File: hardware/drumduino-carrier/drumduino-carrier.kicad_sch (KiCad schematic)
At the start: 49 parts, among them J1 IN A0 CRASH, J10 IN A9 RIDE BELL, J11 IN A10 AUX, J12 IN A11 AUX, J13 IN A12 AUX, J14 IN A13 AUX, J15 IN A14 AUX, J16 HH PEDAL (wiper/VCC/GND), J2 IN A1 HIHAT, J3 IN A2 SNARE, J4 IN A3 KICK, J5 IN A4 TOM1, J6 IN A5 TOM2, J7 IN A6 FLOOR, J8 IN A7 RIDE, J9 IN A8 SN RIM, U1 MEGA2560_PRO

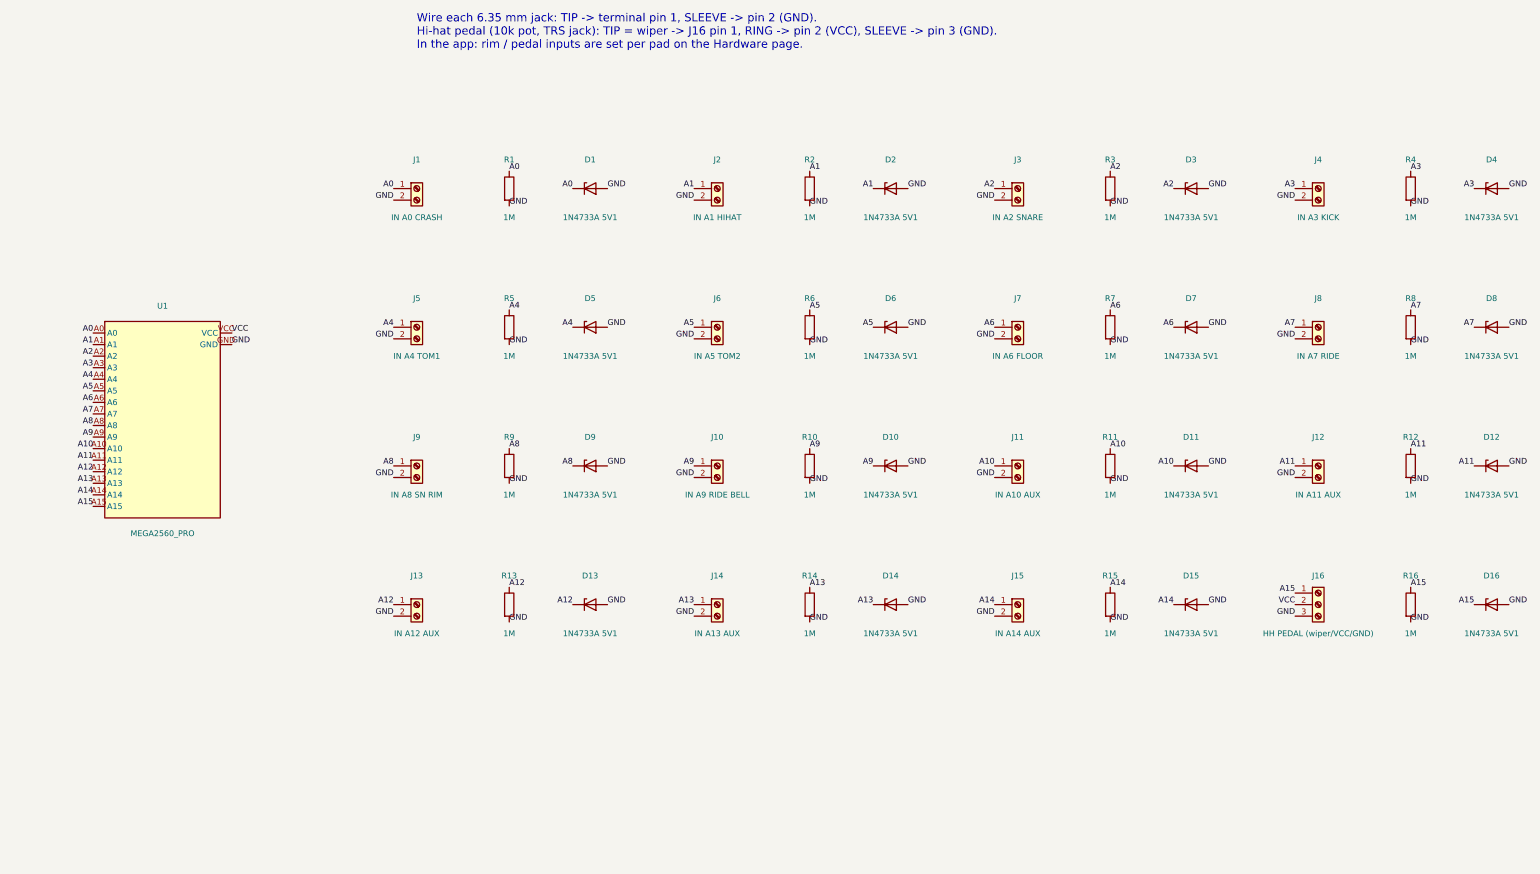
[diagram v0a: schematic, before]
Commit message: Carrier v2: 16 Rean NRJ6HF edge jacks, DC 9V input with 1N5819, local 3D models (incl. Mega 2560 PRO)
Co-Authored-By: Claude Opus 5.5 <noreply@anthropic.com>
Claude-Session: https://claude.ai/code/session_019Dkdmctnzo4hmTgGEA8k6P
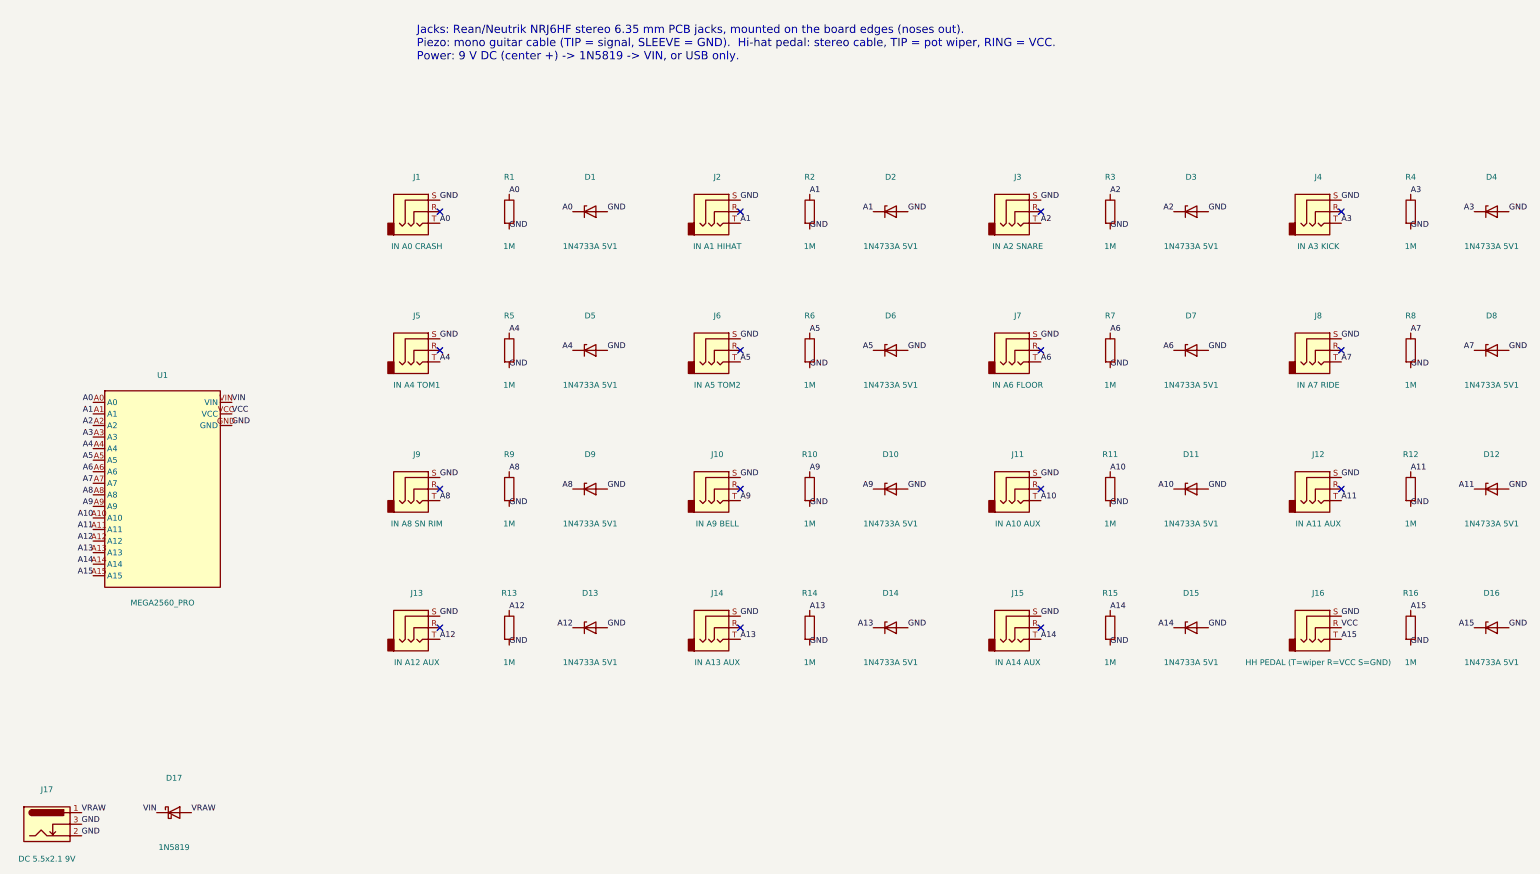
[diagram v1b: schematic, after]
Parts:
- removed J1: IN A0 CRASH, TerminalBlock_Phoenix:TerminalBlock_Phoenix_MKDS-1,5-2-5.08_1x02_P5.08mm_Horizontal, symbol Connector:Screw_Terminal_01x02
- removed J10: IN A9 RIDE BELL, TerminalBlock_Phoenix:TerminalBlock_Phoenix_MKDS-1,5-2-5.08_1x02_P5.08mm_Horizontal, symbol Connector:Screw_Terminal_01x02
- removed J11: IN A10 AUX, TerminalBlock_Phoenix:TerminalBlock_Phoenix_MKDS-1,5-2-5.08_1x02_P5.08mm_Horizontal, symbol Connector:Screw_Terminal_01x02
- removed J12: IN A11 AUX, TerminalBlock_Phoenix:TerminalBlock_Phoenix_MKDS-1,5-2-5.08_1x02_P5.08mm_Horizontal, symbol Connector:Screw_Terminal_01x02
- removed J13: IN A12 AUX, TerminalBlock_Phoenix:TerminalBlock_Phoenix_MKDS-1,5-2-5.08_1x02_P5.08mm_Horizontal, symbol Connector:Screw_Terminal_01x02
- removed J14: IN A13 AUX, TerminalBlock_Phoenix:TerminalBlock_Phoenix_MKDS-1,5-2-5.08_1x02_P5.08mm_Horizontal, symbol Connector:Screw_Terminal_01x02
- removed J15: IN A14 AUX, TerminalBlock_Phoenix:TerminalBlock_Phoenix_MKDS-1,5-2-5.08_1x02_P5.08mm_Horizontal, symbol Connector:Screw_Terminal_01x02
- removed J16: HH PEDAL (wiper/VCC/GND), TerminalBlock_Phoenix:TerminalBlock_Phoenix_MKDS-1,5-3-5.08_1x03_P5.08mm_Horizontal, symbol Connector:Screw_Terminal_01x03
- removed J2: IN A1 HIHAT, TerminalBlock_Phoenix:TerminalBlock_Phoenix_MKDS-1,5-2-5.08_1x02_P5.08mm_Horizontal, symbol Connector:Screw_Terminal_01x02
- removed J3: IN A2 SNARE, TerminalBlock_Phoenix:TerminalBlock_Phoenix_MKDS-1,5-2-5.08_1x02_P5.08mm_Horizontal, symbol Connector:Screw_Terminal_01x02
- removed J4: IN A3 KICK, TerminalBlock_Phoenix:TerminalBlock_Phoenix_MKDS-1,5-2-5.08_1x02_P5.08mm_Horizontal, symbol Connector:Screw_Terminal_01x02
- removed J5: IN A4 TOM1, TerminalBlock_Phoenix:TerminalBlock_Phoenix_MKDS-1,5-2-5.08_1x02_P5.08mm_Horizontal, symbol Connector:Screw_Terminal_01x02
- removed J6: IN A5 TOM2, TerminalBlock_Phoenix:TerminalBlock_Phoenix_MKDS-1,5-2-5.08_1x02_P5.08mm_Horizontal, symbol Connector:Screw_Terminal_01x02
- removed J7: IN A6 FLOOR, TerminalBlock_Phoenix:TerminalBlock_Phoenix_MKDS-1,5-2-5.08_1x02_P5.08mm_Horizontal, symbol Connector:Screw_Terminal_01x02
- removed J8: IN A7 RIDE, TerminalBlock_Phoenix:TerminalBlock_Phoenix_MKDS-1,5-2-5.08_1x02_P5.08mm_Horizontal, symbol Connector:Screw_Terminal_01x02
- removed J9: IN A8 SN RIM, TerminalBlock_Phoenix:TerminalBlock_Phoenix_MKDS-1,5-2-5.08_1x02_P5.08mm_Horizontal, symbol Connector:Screw_Terminal_01x02
- added D17: 1N5819, Diode_THT:D_DO-41_SOD81_P10.16mm_Horizontal, symbol Device:D_Schottky
- added J1: IN A0 CRASH, Connector_Audio:Jack_6.35mm_Neutrik_NRJ6HF_Horizontal, symbol Connector_Audio:AudioJack3
- added J10: IN A9 BELL, Connector_Audio:Jack_6.35mm_Neutrik_NRJ6HF_Horizontal, symbol Connector_Audio:AudioJack3
- added J11: IN A10 AUX, Connector_Audio:Jack_6.35mm_Neutrik_NRJ6HF_Horizontal, symbol Connector_Audio:AudioJack3
- added J12: IN A11 AUX, Connector_Audio:Jack_6.35mm_Neutrik_NRJ6HF_Horizontal, symbol Connector_Audio:AudioJack3
- added J13: IN A12 AUX, Connector_Audio:Jack_6.35mm_Neutrik_NRJ6HF_Horizontal, symbol Connector_Audio:AudioJack3
- added J14: IN A13 AUX, Connector_Audio:Jack_6.35mm_Neutrik_NRJ6HF_Horizontal, symbol Connector_Audio:AudioJack3
- added J15: IN A14 AUX, Connector_Audio:Jack_6.35mm_Neutrik_NRJ6HF_Horizontal, symbol Connector_Audio:AudioJack3
- added J16: HH PEDAL (T=wiper R=VCC S=GND), Connector_Audio:Jack_6.35mm_Neutrik_NRJ6HF_Horizontal, symbol Connector_Audio:AudioJack3
- added J17: DC 5.5x2.1 9V, Connector_BarrelJack:BarrelJack_Horizontal, symbol Connector:Barrel_Jack_Switch
- added J2: IN A1 HIHAT, Connector_Audio:Jack_6.35mm_Neutrik_NRJ6HF_Horizontal, symbol Connector_Audio:AudioJack3
- added J3: IN A2 SNARE, Connector_Audio:Jack_6.35mm_Neutrik_NRJ6HF_Horizontal, symbol Connector_Audio:AudioJack3
- added J4: IN A3 KICK, Connector_Audio:Jack_6.35mm_Neutrik_NRJ6HF_Horizontal, symbol Connector_Audio:AudioJack3
- added J5: IN A4 TOM1, Connector_Audio:Jack_6.35mm_Neutrik_NRJ6HF_Horizontal, symbol Connector_Audio:AudioJack3
- added J6: IN A5 TOM2, Connector_Audio:Jack_6.35mm_Neutrik_NRJ6HF_Horizontal, symbol Connector_Audio:AudioJack3
- added J7: IN A6 FLOOR, Connector_Audio:Jack_6.35mm_Neutrik_NRJ6HF_Horizontal, symbol Connector_Audio:AudioJack3
- added J8: IN A7 RIDE, Connector_Audio:Jack_6.35mm_Neutrik_NRJ6HF_Horizontal, symbol Connector_Audio:AudioJack3
- added J9: IN A8 SN RIM, Connector_Audio:Jack_6.35mm_Neutrik_NRJ6HF_Horizontal, symbol Connector_Audio:AudioJack3
- D1, D10, D11, D12, D13, D14, D15, D16, D2, D3, D4, D5, D6, D7, D8, D9: footprint Diode_THT:D_DO-41_SOD81_P3.81mm_Vertical_AnodeUp -> Diode_THT:D_DO-41_SOD81_P2.54mm_Vertical_AnodeUp
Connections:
- net A0: now also J1.T
- net A1: now also J2.T
- net A10: now also J11.T
- net A11: now also J12.T
- net A12: now also J13.T
- net A13: now also J14.T
- net A14: now also J15.T
- net A15: now also J16.T
- net A2: now also J3.T
- net A3: now also J4.T
- net A4: now also J5.T
- net A5: now also J6.T
- net A6: now also J7.T
- net A7: now also J8.T
- net A8: now also J9.T
- net A9: now also J10.T
- net GND: now also J1.S, J10.S, J11.S, J12.S, J13.S, J14.S, J15.S, J16.S, J17.2, J17.3, J2.S, J3.S, J4.S, J5.S, J6.S, J7.S, J8.S, J9.S
- net VCC: now also J16.R
- new net VIN: D17.1 (K), U1.VIN
- new net VRAW: D17.2 (A), J17.1
- no-connect marks 0 -> 15
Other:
- note added: "Jacks: Rean/Neutrik NRJ6HF stereo 6.35 mm PCB jacks, mounted on the board edges (noses out). Piezo: mono guitar cable (TIP = signal, SLEEVE = GND). Hi-hat pedal: stereo cable, TIP = pot wiper, RING = VCC. Power: 9 V DC (center +) -> 1N5819 -> VIN, or USB only."
- note removed: "Wire each 6.35 mm jack: TIP -> terminal pin 1, SLEEVE -> pin 2 (GND). Hi-hat pedal (10k pot, TRS jack): TIP = wiper -> J16 pin 1, RING -> pin 2 (VCC), SLEEVE -> pin 3 (GND). In the app: rim / pedal inputs are set per pad on the Hardware page."
- title: DrumDuino carrier for Mega 2560 PRO -> DrumDuino carrier v2 for Mega 2560 PRO
